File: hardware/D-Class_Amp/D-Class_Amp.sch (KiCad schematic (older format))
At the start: 0 parts

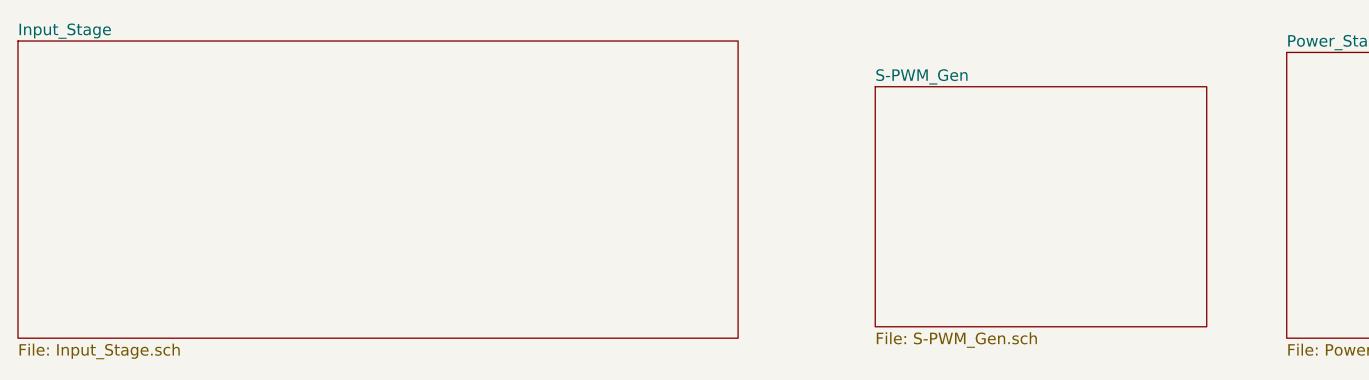
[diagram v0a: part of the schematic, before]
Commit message: edited input filter ground, created schematic for the SPWM generator
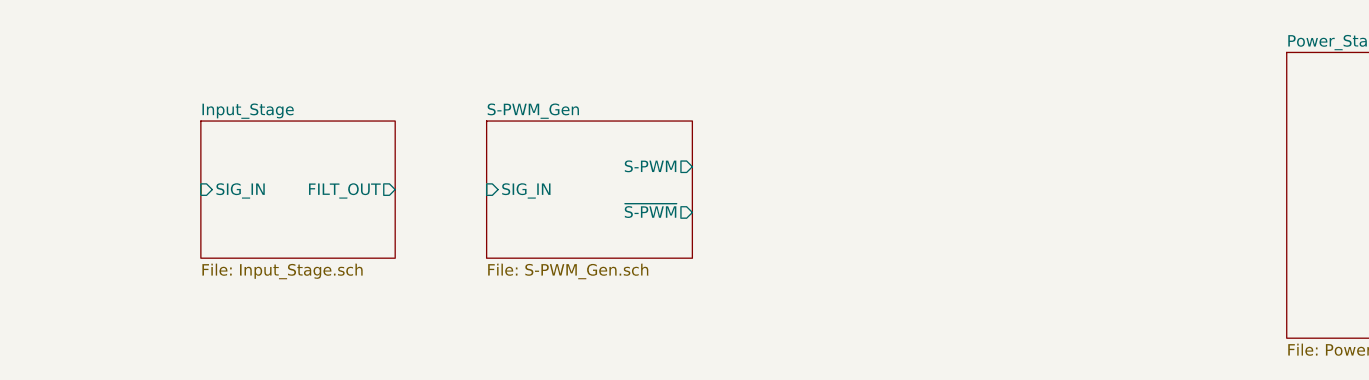
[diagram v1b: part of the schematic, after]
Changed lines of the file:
@@
 $Descr A4 11693 8268
 encoding utf-8
-Sheet 1 4
+Sheet 1 5
 Title ""
 Date ""
@@
 $EndDescr
 $Sheet
-S 1000 3150 3150 1300
+S 1800 3500 850  600
 U 6104907A
 F0 "Input_Stage" 50
 F1 "Input_Stage.sch" 50
+F2 "SIG_IN" I L 1800 3800 50
+F3 "FILT_OUT" O R 2650 3800 50
 $EndSheet
 $Sheet
@@
 $EndSheet
 $Sheet
-S 4750 3350 1450 1050
+S 3050 3500 900  600
 U 61049843
 F0 "S-PWM_Gen" 50
 F1 "S-PWM_Gen.sch" 50
+F2 "S-PWM" O R 3950 3700 50
+F3 "~S-PWM" O R 3950 3900 50
+F4 "SIG_IN" I L 3050 3800 50
 $EndSheet
 $EndSCHEMATC

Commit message: edits
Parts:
- added LS?: Speaker, symbol Device:Speaker
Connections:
- new net Output_Filter/SPEAKER_OUT: LS?.1
- new net Output_Filter/~SPEAKER_OUT: LS?.2
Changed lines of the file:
@@
 $EndSheet
 $Sheet
-S 6550 3200 2350 1250
+S 4300 3500 850  600
 U 610497A4
 F0 "Power_Stage" 50
 F1 "Power_Stage.sch" 50
+F2 "S-PWM" I L 4300 3700 50
+F3 "~S-PWM" I L 4300 3900 50
+F4 "P_OUT" O R 5150 3700 50
+F5 "~P_OUT" O R 5150 3900 50
 $EndSheet
 $Sheet
-S 9250 3500 1050 750
+S 5500 3400 1050 750
 U 610497C9
-F0 "Sheet610497C8" 50
+F0 "Output_Filter" 50
 F1 "Output_Filter.sch" 50
+F2 "SIG_IN" I L 5500 3700 50
+F3 "~SIG_IN" I L 5500 3900 50
+F4 "SPEAKER_OUT" O R 6550 3700 50
+F5 "~SPEAKER_OUT" O R 6550 3900 50
 $EndSheet
 $Sheet
@@
 F4 "SIG_IN" I L 3050 3800 50
 $EndSheet
+Wire Wire Line
+	2650 3800 3050 3800
+Wire Wire Line
+	3950 3700 4300 3700
+Wire Wire Line
+	3950 3900 4300 3900
+$Comp
+L Device:Speaker LS?
+U 1 1 61193870
+P 6925 3750
+F 0 "LS?" H 7095 3746 50  0000 L CNN
+F 1 "Speaker" H 7095 3655 50  0000 L CNN
+F 2 "" H 6925 3550 50  0001 C CNN
+F 3 "~" H 6915 3700 50  0001 C CNN
+	1    6925 3750
+	1    0    0    -1
+$EndComp
+Wire Wire Line
+	5150 3700 5500 3700
+Wire Wire Line
+	5150 3900 5500 3900
+Wire Wire Line
+	6550 3700 6650 3700
+Wire Wire Line
+	6650 3700 6650 3750
+Wire Wire Line
+	6650 3750 6725 3750
+Wire Wire Line
+	6550 3900 6650 3900
+Wire Wire Line
+	6650 3900 6650 3850
+Wire Wire Line
+	6650 3850 6725 3850
 $EndSCHEMATC

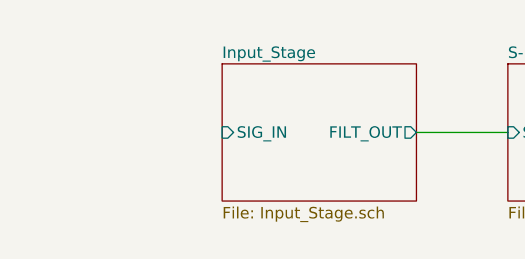
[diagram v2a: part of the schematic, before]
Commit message: Added an input barel jack
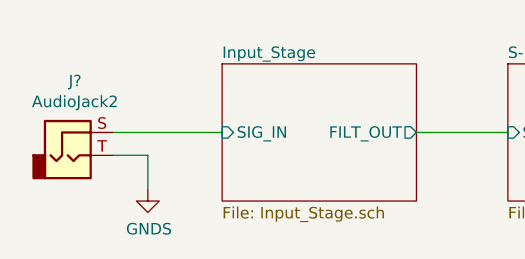
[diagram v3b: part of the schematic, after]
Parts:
- added J?: AudioJack2, symbol Connector:AudioJack2
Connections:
- net Input_Stage/SIG_IN: now also J?.S
- new net GNDS: J?.T
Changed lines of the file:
@@
 Wire Wire Line
 	6650 3850 6725 3850
+$Comp
+L Connector:AudioJack2 J?
+U 1 1 611DD9A4
+P 1125 3900
+F 0 "J?" H 1157 4225 50  0000 C CNN
+F 1 "AudioJack2" H 1157 4134 50  0000 C CNN
+F 2 "" H 1125 3900 50  0001 C CNN
+F 3 "~" H 1125 3900 50  0001 C CNN
+	1    1125 3900
+	1    0    0    -1
+$EndComp
+Wire Wire Line
+	1325 3800 1800 3800
+$Comp
+L power:GNDS #PWR?
+U 1 1 611DE882
+P 1475 4050
+F 0 "#PWR?" H 1475 3800 50  0001 C CNN
+F 1 "GNDS" H 1480 3877 50  0000 C CNN
+F 2 "" H 1475 4050 50  0001 C CNN
+F 3 "" H 1475 4050 50  0001 C CNN
+	1    1475 4050
+	1    0    0    -1
+$EndComp
+Wire Wire Line
+	1325 3900 1475 3900
+Wire Wire Line
+	1475 3900 1475 4050
 $EndSCHEMATC

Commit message: single side
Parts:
- added NT1: Net-Tie_2, symbol Device:Net-Tie_2
- gave numbers to parts that had none: 2
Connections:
- net GNDS: now also NT1.2
- new net GND: NT1.1
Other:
- moved on the sheet: J1, LS1
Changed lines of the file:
@@
 $EndDescr
 $Sheet
-S 1800 3500 850  600
+S 5225 1150 850  600
 U 6104907A
 F0 "Input_Stage" 50
 F1 "Input_Stage.sch" 50
-F2 "SIG_IN" I L 1800 3800 50
-F3 "FILT_OUT" O R 2650 3800 50
+F2 "SIG_IN" I L 5225 1450 50
+F3 "FILT_OUT" O R 6075 1450 50
 $EndSheet
 $Sheet
-S 4300 3500 850  600
+S 7725 1150 850  600
 U 610497A4
 F0 "Power_Stage" 50
 F1 "Power_Stage.sch" 50
-F2 "S-PWM" I L 4300 3700 50
-F3 "~S-PWM" I L 4300 3900 50
-F4 "P_OUT" O R 5150 3700 50
-F5 "~P_OUT" O R 5150 3900 50
+F2 "S-PWM" I L 7725 1350 50
+F3 "~S-PWM" I L 7725 1550 50
+F4 "P_OUT" O R 8575 1350 50
+F5 "~P_OUT" O R 8575 1550 50
 $EndSheet
 $Sheet
-S 5500 3400 1050 750
+S 8925 1150 1000 600
 U 610497C9
 F0 "Output_Filter" 50
 F1 "Output_Filter.sch" 50
-F2 "SIG_IN" I L 5500 3700 50
-F3 "~SIG_IN" I L 5500 3900 50
-F4 "SPEAKER_OUT" O R 6550 3700 50
-F5 "~SPEAKER_OUT" O R 6550 3900 50
+F2 "SIG_IN" I L 8925 1350 50
+F3 "~SIG_IN" I L 8925 1550 50
+F4 "SPEAKER_OUT" O R 9925 1350 50
+F5 "~SPEAKER_OUT" O R 9925 1550 50
 $EndSheet
 $Sheet
-S 3050 3500 900  600
+S 6475 1150 900  600
 U 61049843
 F0 "S-PWM_Gen" 50
 F1 "S-PWM_Gen.sch" 50
-F2 "S-PWM" O R 3950 3700 50
-F3 "~S-PWM" O R 3950 3900 50
-F4 "SIG_IN" I L 3050 3800 50
+F2 "S-PWM" O R 7375 1350 50
+F3 "~S-PWM" O R 7375 1550 50
+F4 "SIG_IN" I L 6475 1450 50
 $EndSheet
 Wire Wire Line
-	2650 3800 3050 3800
+	6075 1450 6475 1450
 Wire Wire Line
-	3950 3700 4300 3700
+	7375 1350 7725 1350
 Wire Wire Line
-	3950 3900 4300 3900
+	7375 1550 7725 1550
 $Comp
-L Device:Speaker LS?
+L Device:Speaker LS1
 U 1 1 61193870
-P 6925 3750
-F 0 "LS?" H 7095 3746 50  0000 L CNN
-F 1 "Speaker" H 7095 3655 50  0000 L CNN
-F 2 "" H 6925 3550 50  0001 C CNN
-F 3 "~" H 6915 3700 50  0001 C CNN
-	1    6925 3750
+P 10300 1400
+F 0 "LS1" H 10470 1396 50  0000 L CNN
+F 1 "Speaker" H 10470 1305 50  0000 L CNN
+F 2 "" H 10300 1200 50  0001 C CNN
+F 3 "~" H 10290 1350 50  0001 C CNN
+	1    10300 1400
 	1    0    0    -1
 $EndComp
 Wire Wire Line
-	5150 3700 5500 3700
+	8575 1350 8925 1350
 Wire Wire Line
-	5150 3900 5500 3900
+	9925 1350 10025 1350
 Wire Wire Line
-	6550 3700 6650 3700
+	10025 1350 10025 1400
 Wire Wire Line
-	6650 3700 6650 3750
+	10025 1400 10100 1400
 Wire Wire Line
-	6650 3750 6725 3750
+	9925 1550 10025 1550
 Wire Wire Line
-	6550 3900 6650 3900
+	10025 1550 10025 1500
 Wire Wire Line
-	6650 3900 6650 3850
-Wire Wire Line
-	6650 3850 6725 3850
+	10025 1500 10100 1500
 $Comp
-L Connector:AudioJack2 J?
+L Connector:AudioJack2 J1
 U 1 1 611DD9A4
-P 1125 3900
-F 0 "J?" H 1157 4225 50  0000 C CNN
-F 1 "AudioJack2" H 1157 4134 50  0000 C CNN
-F 2 "" H 1125 3900 50  0001 C CNN
-F 3 "~" H 1125 3900 50  0001 C CNN
-	1    1125 3900
+P 4550 1550
+F 0 "J1" H 4582 1875 50  0000 C CNN
+F 1 "AudioJack2" H 4582 1784 50  0000 C CNN
+F 2 "" H 4550 1550 50  0001 C CNN
+F 3 "~" H 4550 1550 50  0001 C CNN
+	1    4550 1550
 	1    0    0    -1
 $EndComp
 Wire Wire Line
-	1325 3800 1800 3800
+	4750 1450 5225 1450
 $Comp
 L power:GNDS #PWR?
 U 1 1 611DE882
-P 1475 4050
-F 0 "#PWR?" H 1475 3800 50  0001 C CNN
-F 1 "GNDS" H 1480 3877 50  0000 C CNN
-F 2 "" H 1475 4050 50  0001 C CNN
-F 3 "" H 1475 4050 50  0001 C CNN
-	1    1475 4050
+P 4900 1700
+F 0 "#PWR?" H 4900 1450 50  0001 C CNN
+F 1 "GNDS" H 4905 1527 50  0000 C CNN
+F 2 "" H 4900 1700 50  0001 C CNN
+F 3 "" H 4900 1700 50  0001 C CNN
+	1    4900 1700
 	1    0    0    -1
 $EndComp
 Wire Wire Line
-	1325 3900 1475 3900
+	4750 1550 4900 1550
 Wire Wire Line
-	1475 3900 1475 4050
+	4900 1550 4900 1700
+Wire Wire Line
+	8575 1550 8925 1550
+Wire Notes Line
+	4175 475  4175 1975
+Wire Notes Line
+	4175 1975 11250 1975
+$Comp
+L power:GNDS #PWR?
+U 1 1 612A4FBB
+P 2150 1300
+F 0 "#PWR?" H 2150 1050 50  0001 C CNN
+F 1 "GNDS" H 2155 1127 50  0000 C CNN
+F 2 "" H 2150 1300 50  0001 C CNN
+F 3 "" H 2150 1300 50  0001 C CNN
+	1    2150 1300
+	1    0    0    -1
+$EndComp
+$Comp
+L power:GND #PWR?
+U 1 1 612A56C1
+P 1800 1300
+F 0 "#PWR?" H 1800 1050 50  0001 C CNN
+F 1 "GND" H 1805 1127 50  0000 C CNN
+F 2 "" H 1800 1300 50  0001 C CNN
+F 3 "" H 1800 1300 50  0001 C CNN
+	1    1800 1300
+	1    0    0    -1
+$EndComp
+$Comp
+L Device:Net-Tie_2 NT1
+U 1 1 612A676E
+P 1975 1225
+F 0 "NT1" H 1975 1406 50  0000 C CNN
+F 1 "Net-Tie_2" H 1975 1315 50  0000 C CNN
+F 2 "" H 1975 1225 50  0001 C CNN
+F 3 "~" H 1975 1225 50  0001 C CNN
+	1    1975 1225
+	1    0    0    -1
+$EndComp
+Wire Wire Line
+	1800 1300 1800 1225
+Wire Wire Line
+	1800 1225 1875 1225
+Wire Wire Line
+	2075 1225 2150 1225
+Wire Wire Line
+	2150 1225 2150 1300
 $EndSCHEMATC

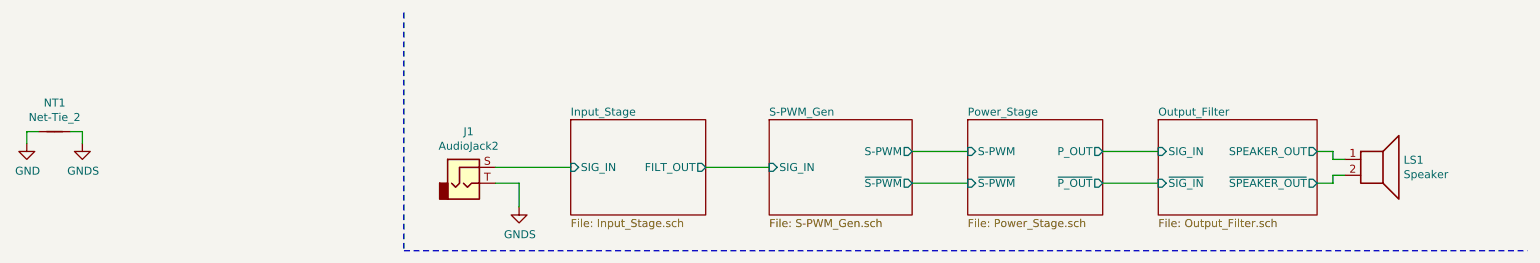
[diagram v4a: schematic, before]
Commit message: Added input bias circuit and gain stage to input-stage schematic.
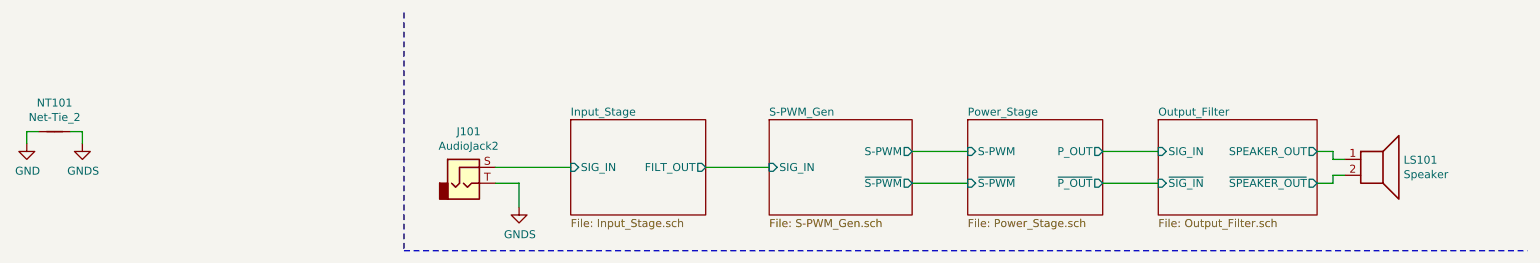
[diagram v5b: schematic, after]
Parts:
- renumbered J1 to J101, LS1 to LS101, NT1 to NT101
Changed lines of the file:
@@
 	7375 1550 7725 1550
 $Comp
-L Device:Speaker LS1
+L Device:Speaker LS101
 U 1 1 61193870
 P 10300 1400
-F 0 "LS1" H 10470 1396 50  0000 L CNN
+F 0 "LS101" H 10470 1396 50  0000 L CNN
 F 1 "Speaker" H 10470 1305 50  0000 L CNN
 F 2 "" H 10300 1200 50  0001 C CNN
@@
 	10025 1500 10100 1500
 $Comp
-L Connector:AudioJack2 J1
+L Connector:AudioJack2 J101
 U 1 1 611DD9A4
 P 4550 1550
-F 0 "J1" H 4582 1875 50  0000 C CNN
+F 0 "J101" H 4582 1875 50  0000 C CNN
 F 1 "AudioJack2" H 4582 1784 50  0000 C CNN
 F 2 "" H 4550 1550 50  0001 C CNN
@@
 	4750 1450 5225 1450
 $Comp
-L power:GNDS #PWR?
+L power:GNDS #PWR0103
 U 1 1 611DE882
 P 4900 1700
-F 0 "#PWR?" H 4900 1450 50  0001 C CNN
+F 0 "#PWR0103" H 4900 1450 50  0001 C CNN
 F 1 "GNDS" H 4905 1527 50  0000 C CNN
 F 2 "" H 4900 1700 50  0001 C CNN
@@
 	4175 1975 11250 1975
 $Comp
-L power:GNDS #PWR?
+L power:GNDS #PWR0102
 U 1 1 612A4FBB
 P 2150 1300
-F 0 "#PWR?" H 2150 1050 50  0001 C CNN
+F 0 "#PWR0102" H 2150 1050 50  0001 C CNN
 F 1 "GNDS" H 2155 1127 50  0000 C CNN
 F 2 "" H 2150 1300 50  0001 C CNN
@@
 $EndComp
 $Comp
-L power:GND #PWR?
+L power:GND #PWR0101
 U 1 1 612A56C1
 P 1800 1300
-F 0 "#PWR?" H 1800 1050 50  0001 C CNN
+F 0 "#PWR0101" H 1800 1050 50  0001 C CNN
 F 1 "GND" H 1805 1127 50  0000 C CNN
 F 2 "" H 1800 1300 50  0001 C CNN
@@
 $EndComp
 $Comp
-L Device:Net-Tie_2 NT1
+L Device:Net-Tie_2 NT101
 U 1 1 612A676E
 P 1975 1225
-F 0 "NT1" H 1975 1406 50  0000 C CNN
+F 0 "NT101" H 1975 1406 50  0000 C CNN
 F 1 "Net-Tie_2" H 1975 1315 50  0000 C CNN
 F 2 "" H 1975 1225 50  0001 C CNN
